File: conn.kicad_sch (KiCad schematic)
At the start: 44 parts, among them J401 XT30, J402 MX3.0 2x2, J403 MX3.0 2x2, J404 USB-C, J405 USB-C, J406 USB-A, Q401 CJAC70P06, Q402 CJAC70P06, Q403 AO3400A, Q404 AO3400A, U401 CH334F, U402 USBLC6-2SC6, U403 USBLC6-2SC6, U404 USBLC6-2SC6

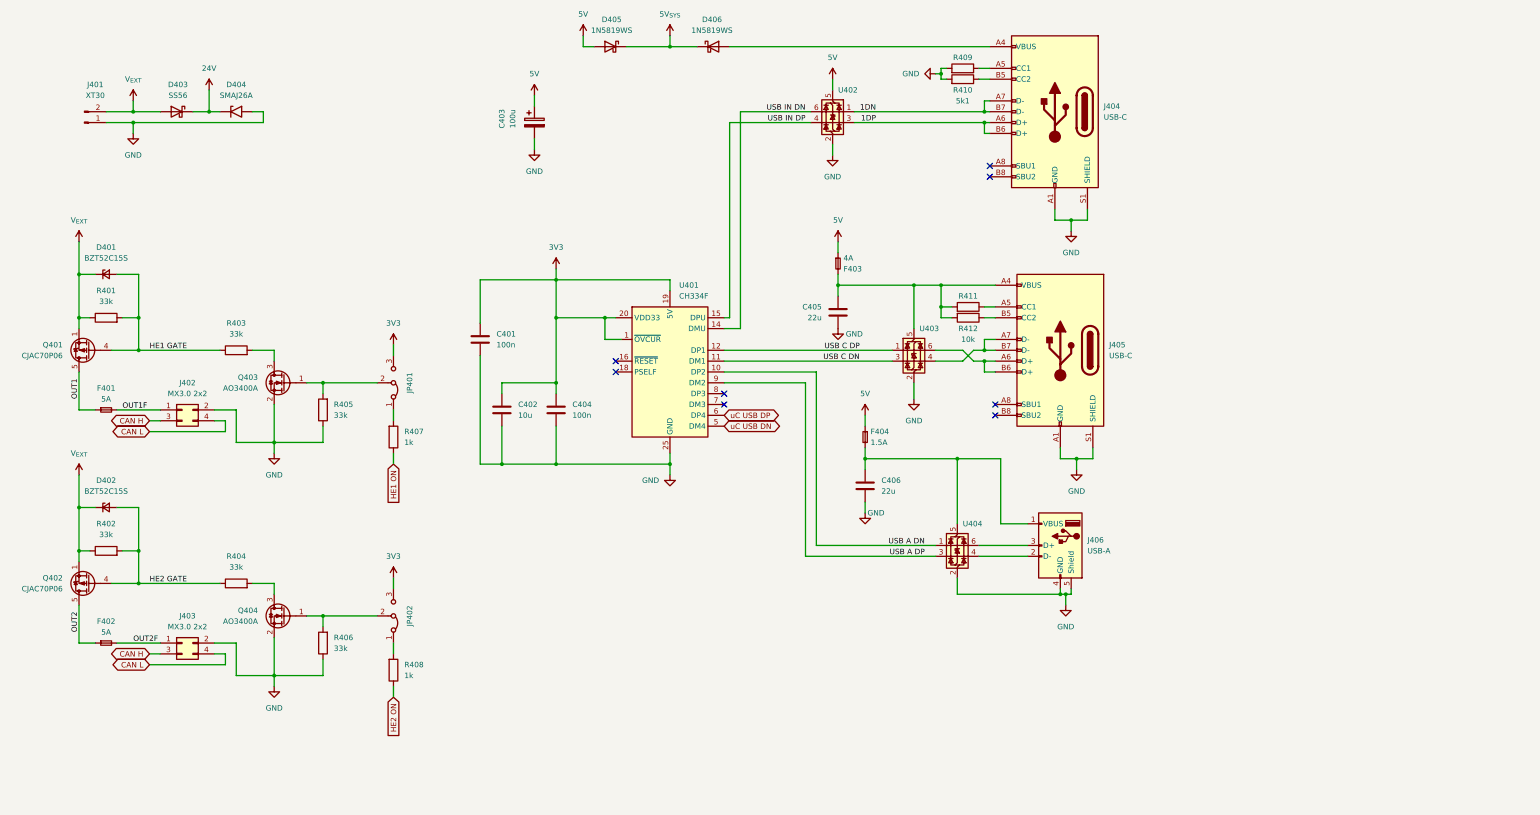
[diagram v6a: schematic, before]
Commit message: docs: Update unreleased changes in changelog and README
- Fixed USB hub controller (U401/CH334): XO pin connected to GND for crystal-less operation
- Fixed DC/DC converter (U202/XR76208): Enable circuit changed to Zener diode for 12V operation
- Fixed USB outputs: Replaced fuses with TPS2557 power distribution switches for backfeed protection
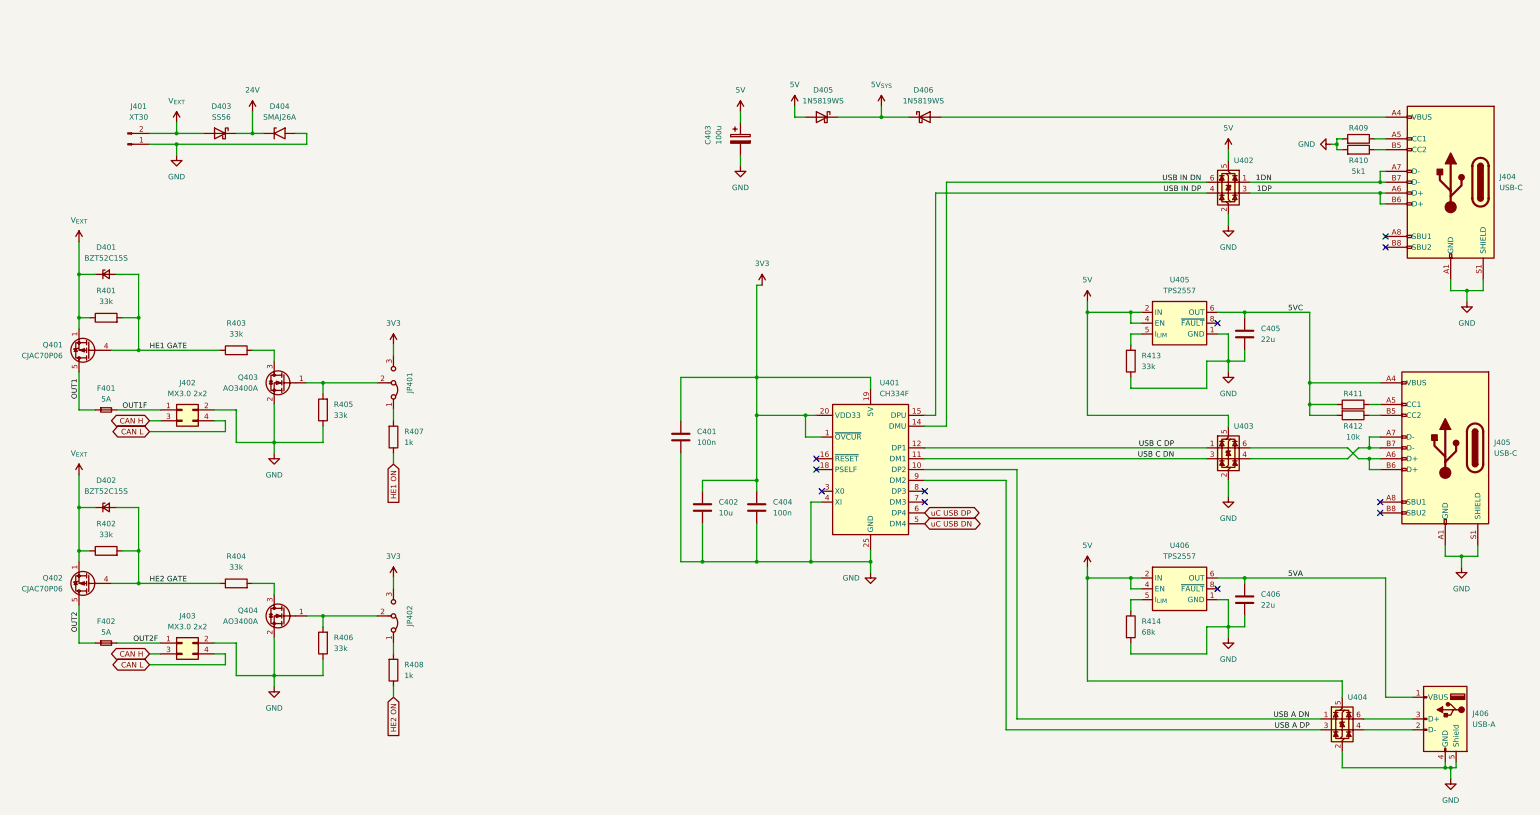
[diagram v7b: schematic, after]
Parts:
- removed F403: 4A, Fuse:Fuse_0805_2012Metric, symbol Device:Fuse_Small
- removed F404: 1.5A, Fuse:Fuse_0805_2012Metric, symbol Device:Fuse_Small
- added R413: 33k, Resistor_SMD:R_0402_1005Metric, symbol Device:R
- added R414: 68k, Resistor_SMD:R_0603_1608Metric, symbol Device:R
- added U405, U406: TPS2557, project:S-PVSON-N8, symbol project:TPS2557
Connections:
- net 5V: now also U403.5 (VBUS), U404.5 (VBUS), U405.2 (IN), U405.3 (IN), U405.4 (EN), U406.2 (IN), U406.3 (IN), U406.4 (EN)
- net GND: now also U401.4 (XI), R413.1, R414.2, U405.1 (GND), U405.9 (GND), U406.1 (GND), U406.9 (GND)
- net 5VC: now reaches C405.1, J405.A4 (VBUS), J405.A9 (VBUS), J405.B4 (VBUS), J405.B9 (VBUS), R411.2, R412.2
- net 5VC: now also U405.6 (OUT), U405.7 (OUT); no longer U403.5 (VBUS)
- net 5VA: now reaches C406.1, J406.1 (VBUS)
- net 5VA: now also U406.6 (OUT), U406.7 (OUT); no longer U404.5 (VBUS)
- new net: R414.1, U406.5 (I_{LIM})
- new net: R413.2, U405.5 (I_{LIM})
- no-connect marks 8 -> 11
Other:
- moved on the sheet: C401, C402, C403, C404, C405, C406, D403, D404, D405, D406, J401, J404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
